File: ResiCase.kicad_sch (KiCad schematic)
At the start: 239 parts, among them J1 Power, J10 Conn_02x07_Odd_Even, J2 Analog, J3 Analog, J4 Digital, J5 PWM, J6 PWM, J7 Communication, J8 Conn_02x03_Odd_Even, J9 Conn_02x14_Odd_Even, Q1 BC516, Q10 BC516, Q11 BC516, Q12 BC516, Q13 BC516, Q14 BC516, Q2 BC516, Q3 BC516, Q4 BC516, Q5 BC516, Q6 BC516, Q7 BC516, Q8 BC516, Q9 BC516, U1 L7809, U10 LM2902, U11 LM2902, U12 LM2902, U13 LM2902, U14 LM2902, U15 LM2902, U16 LM2902, U17 LM2902, U18 LM2902, U2 ULN2004A, U3 ULN2004A, U4 ULN2004A, U5 LM2902, U6 LM2902, U7 LM2902, U8 LM2902, U9 LM2902

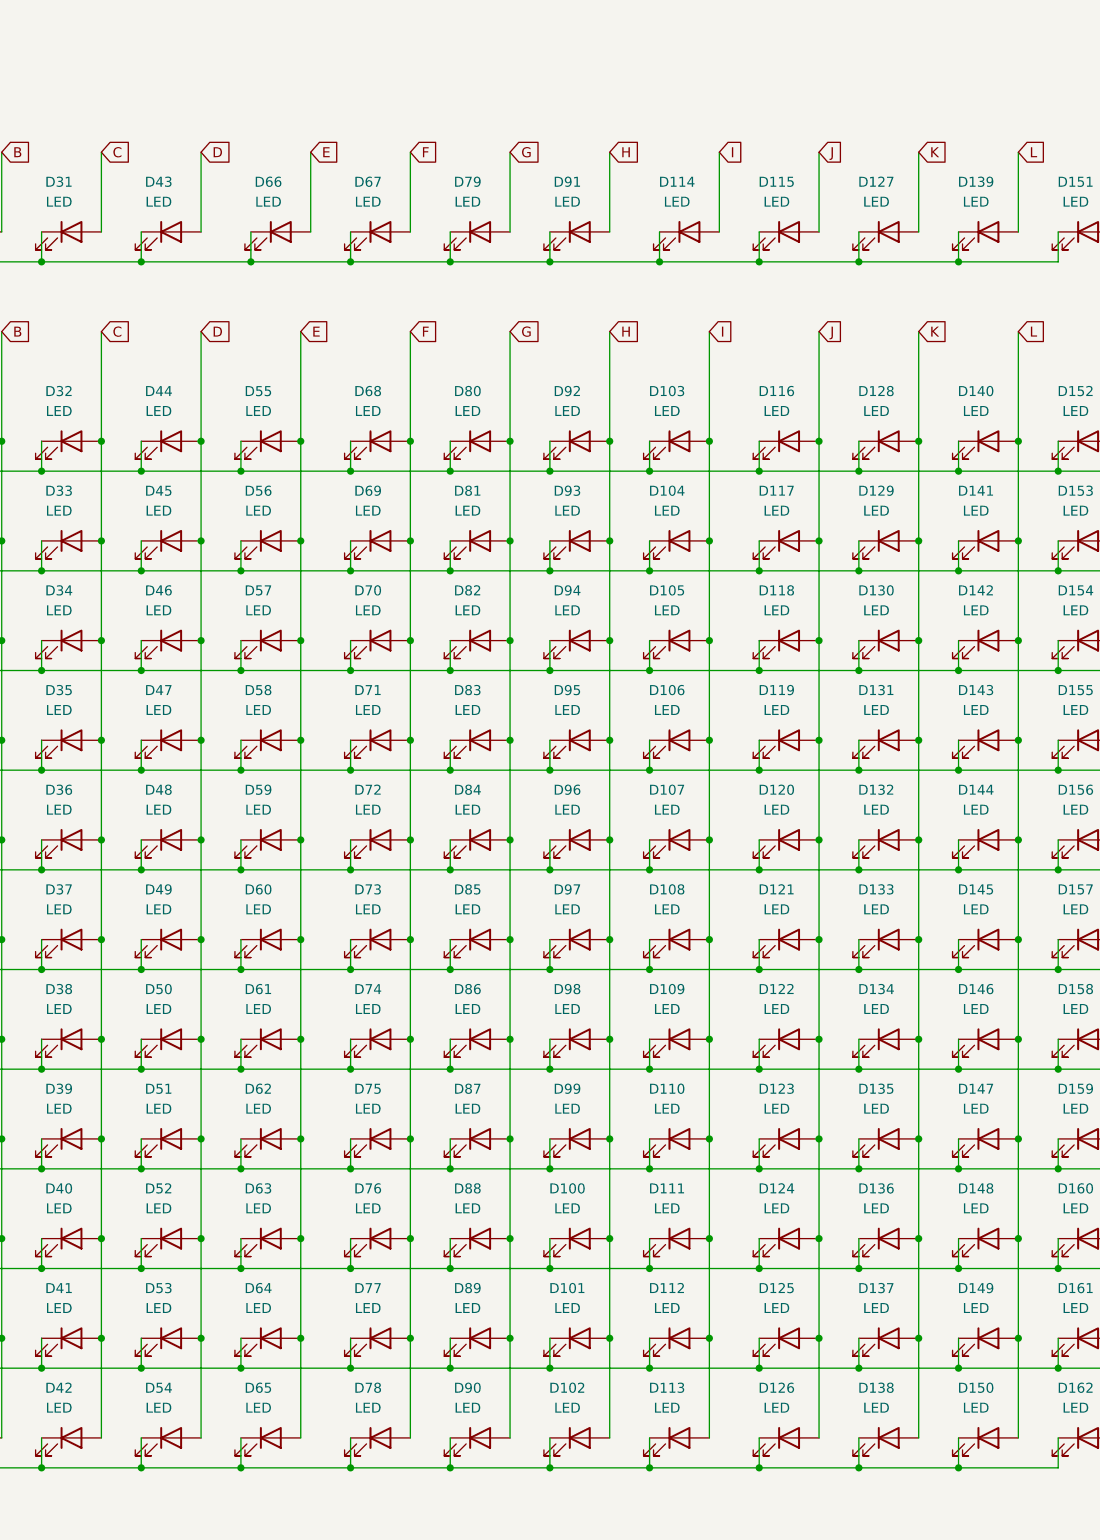
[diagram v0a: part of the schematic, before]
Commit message: Excluded pots and LEDs from board
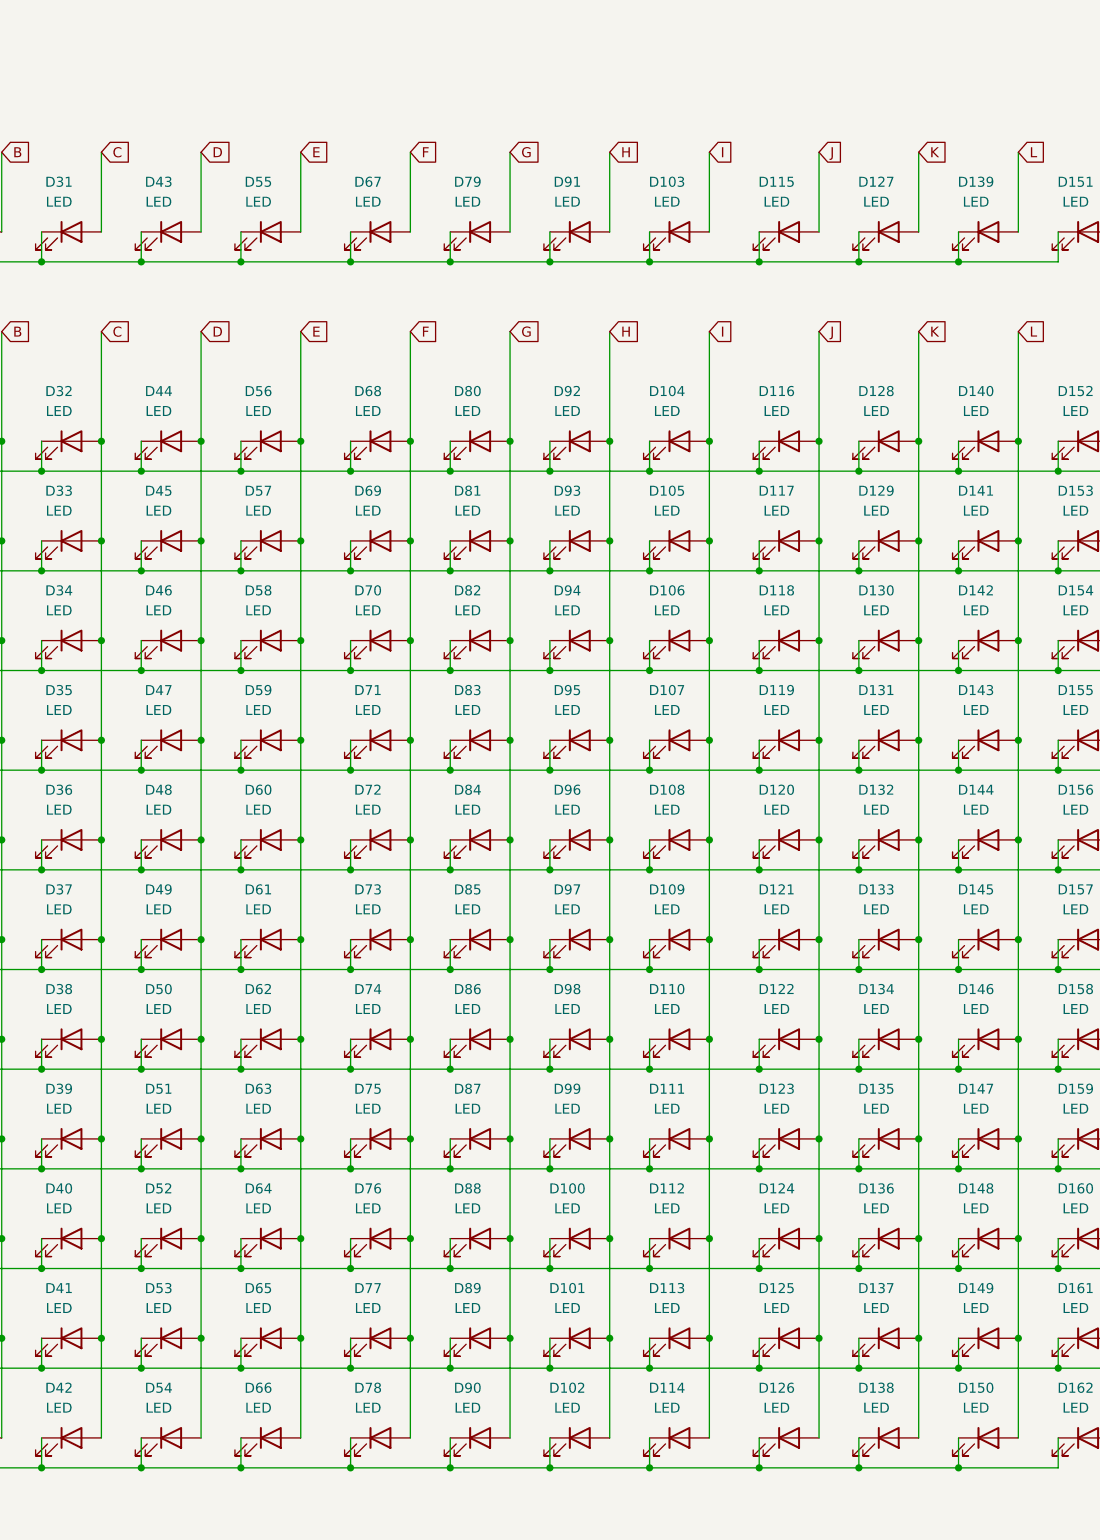
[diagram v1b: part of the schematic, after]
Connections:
- net 0: now also D103.1 (K), D55.1 (K); no longer D114.1 (K), D66.1 (K)
- net 1: now also D104.1 (K), D56.1 (K); no longer D103.1 (K), D55.1 (K)
- net 10: now also D113.1 (K), D65.1 (K); no longer D112.1 (K), D64.1 (K)
- net 11: now also D114.1 (K), D66.1 (K); no longer D113.1 (K), D65.1 (K)
- net 2: now also D105.1 (K), D57.1 (K); no longer D104.1 (K), D56.1 (K)
- net 3: now also D106.1 (K), D58.1 (K); no longer D105.1 (K), D57.1 (K)
- net 4: now also D107.1 (K), D59.1 (K); no longer D106.1 (K), D58.1 (K)
- net 5: now also D108.1 (K), D60.1 (K); no longer D107.1 (K), D59.1 (K)
- net 6: now also D109.1 (K), D61.1 (K); no longer D108.1 (K), D60.1 (K)
- net 7: now also D110.1 (K), D62.1 (K); no longer D109.1 (K), D61.1 (K)
- net 8: now also D111.1 (K), D63.1 (K); no longer D110.1 (K), D62.1 (K)
- net 9: now also D112.1 (K), D64.1 (K); no longer D111.1 (K), D63.1 (K)
